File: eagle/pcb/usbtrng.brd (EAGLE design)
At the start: 61 x 30.5 mm, 37 parts, among them IC1 FT232RL, IC2 ATMEGA88, IC3 XC9572XL VQ44, IC4 LT1763CS8-3.3, J1 CON_HEADER_2X03-PTH, J2 CON_HEADER_1X06-PTH, J3 CON_HEADER_1X05-PTH, J5 CON_HEADER_1X01-PTH, J7 CON_HEADER_1X01-PTH, J8 CON_HEADER_1X01-PTH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

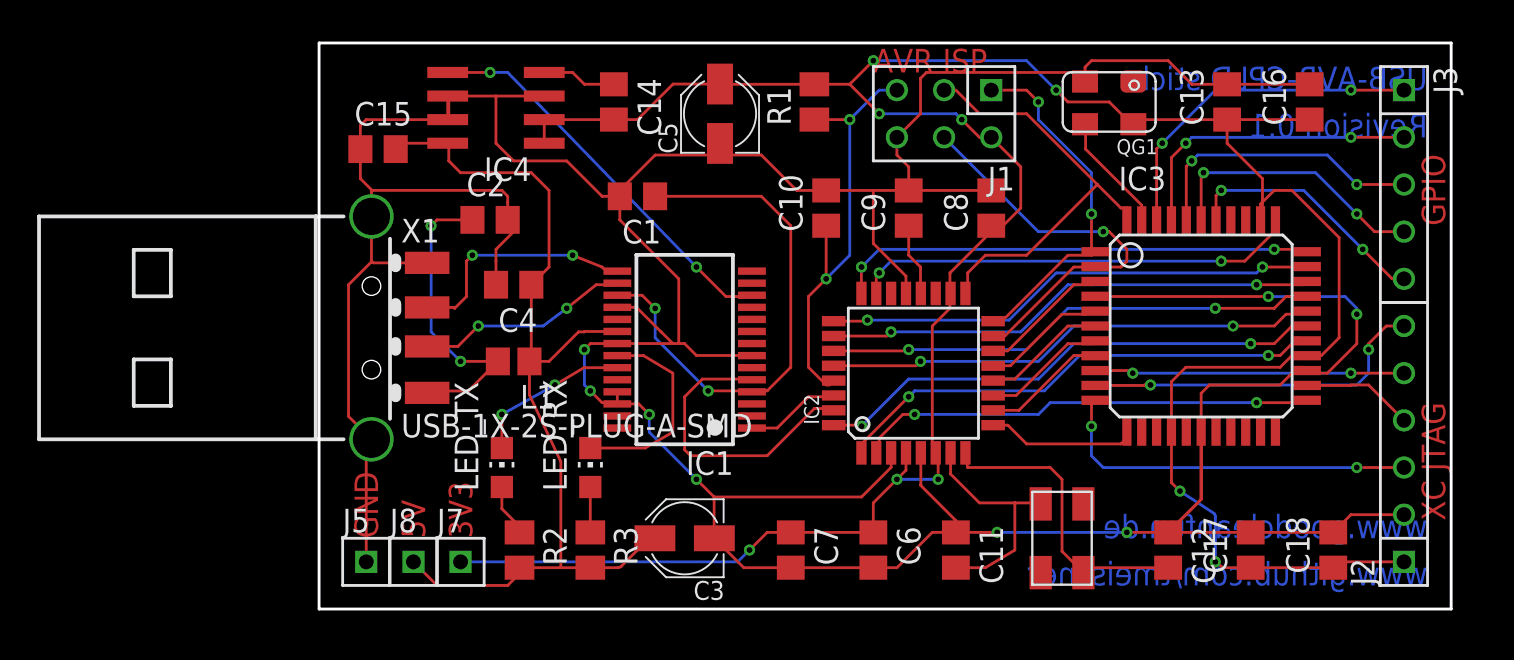
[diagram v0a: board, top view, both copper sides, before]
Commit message: major revision of board layout
* better signal routing around ft232rl
* better placement of blockng capacitors
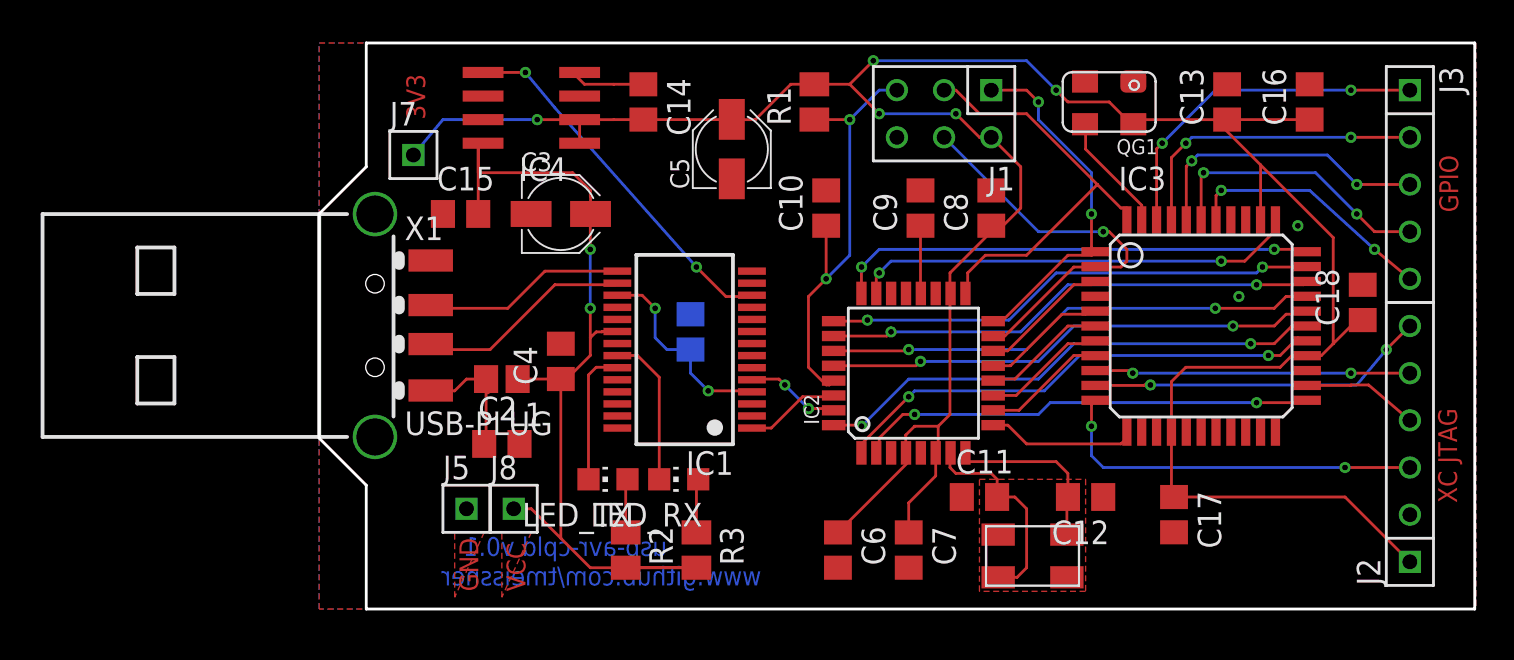
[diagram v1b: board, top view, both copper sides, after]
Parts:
- X1: value USB-1X-2S-PLUG-A-SMD -> USB-PLUG
- moved J7 22.1 mm to (5.08, 24.4)
- moved C3 18.7 mm to (13.0, 21.3), turned to 0 degrees
- moved C18 13.4 mm to (56.2, 16.5)
- moved C2 12.1 mm to (9.84, 8.89)
- moved C1 7.84 mm to (20.0, 14.9), flipped to the bottom, turned to 90 degrees
- moved C7 6.35 mm to (31.8, 3.17)
- moved J5 6.11 mm to (7.94, 5.40)
- moved J8 6.11 mm to (10.5, 5.40)
- moved LED_TX 5.75 mm to (15.6, 6.99), turned to 90 degrees
- moved R2 5.72 mm to (16.5, 3.17)
- moved R3 5.71 mm to (20.3, 3.17)
- moved C15 5.65 mm to (7.62, 21.3)
- moved C12 5.28 mm to (41.3, 6.03), turned to 180 degrees
- moved C4 4.85 mm to (13.0, 13.3), turned to 90 degrees
- moved LED_RX 4.80 mm to (19.4, 6.99), turned to 90 degrees
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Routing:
- net GND: track 257.4 -> 0.00 mm, vias 8 -> 2
- net N$6: track 28.5 -> 11.1 mm
- net FT_RX: track 16.1 -> 5.38 mm, vias 0 -> 2
- net N$4: track 18.0 -> 7.73 mm, vias 2 -> 0
- net +3V3: track 155.5 -> 147.6 mm, vias 9 -> 5
- net N$11: track 16.3 -> 9.50 mm
- net N$9: track 11.1 -> 8.24 mm
- net N$1: track 12.9 -> 11.2 mm, vias 2 -> 0
- net FT_#SLEEP: track 21.5 -> 19.9 mm
- net VCC: track 52.9 -> 51.4 mm, vias 0 -> 2
- net N$8: track 8.69 -> 7.35 mm, vias 2 -> 0
- net N$10: track 12.6 -> 11.6 mm
- net N$5: track 2.45 -> 3.32 mm
- net N$7: track 3.60 -> 2.96 mm
- net XC_TMS: track 18.9 -> 18.4 mm
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- added copper zone on layer 1, net GND
- added copper zone on layer 16, net GND
- added copper zone on layer 1, net N$19
- added copper zone on layer 1, net N$20
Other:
- board size 61 x 30.5 mm -> 62.2 x 30.5 mm
- board text added: "VCC"
- board text added: "usb-avr-cpld v0.1"
- board text removed: "5V"
- board text removed: "AVR ISP"
- board text removed: "Revision 0.1"
- board text removed: "USB-AVR-CPLD stick"
- board text removed: "www.goodcleanfun.de"

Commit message: This is the revision, that is manufactured at q-print, v.0.1
* integrated 32 Mbit SPI-Flash, connected to the CPLD
* The rx/tx leds are now powerd by VCCIO
* further layout optimisations
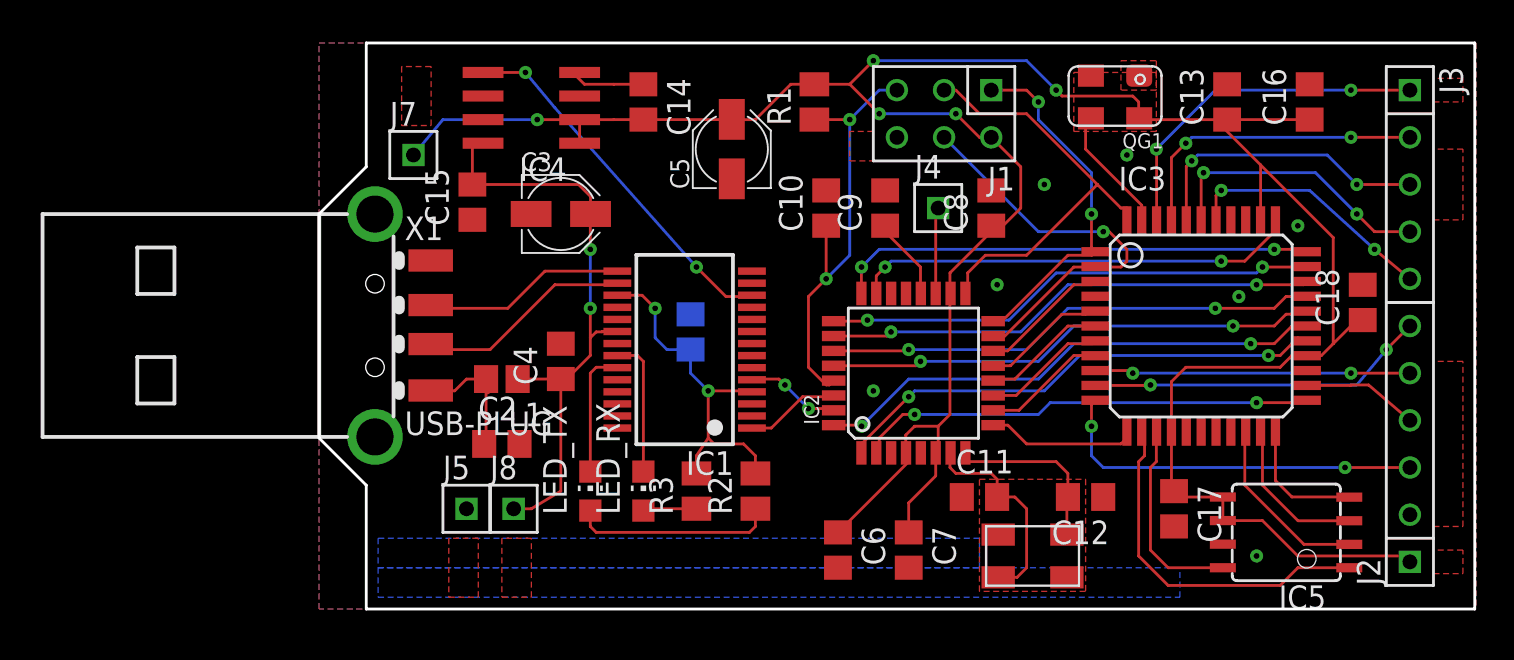
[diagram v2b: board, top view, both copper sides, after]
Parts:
- added IC5: AT45DB161D-SU, atmel:8S2
- added J4: CON_HEADER_1X01-PTH, dp_devices:M1X1
- R2, R3: value 1k -> 68
- moved R2 7.67 mm to (23.5, 6.35), turned to 90 degrees
- moved R3 3.17 mm to (20.3, 6.35), turned to 90 degrees
- moved LED_RX 2.01 mm to (17.5, 6.35), turned to 0 degrees
- moved C9 1.90 mm to (30.5, 21.6)
- moved LED_TX 1.14 mm to (14.6, 6.35), turned to 0 degrees
- moved C15 0.90 mm to (8.26, 21.9), turned to 90 degrees
- moved QG1 0.45 mm to (42.9, 27.6)
- moved C17 0.32 mm to (46.0, 5.40)
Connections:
- new net FLASH_#CS: IC3.22, IC5.4
- new net FLASH_#RST: IC3.21, IC5.3
- new net FLASH_MISO: IC3.14, IC5.8
- new net FLASH_MOSI: IC3.13, IC5.1
- new net FLASH_SCK: IC3.20, IC5.2
- new net N$18: IC2.19, J4.1
- net +3V3: now also IC5.5, IC5.6
- net GND: now also IC5.7
- net N$6: now also R2.2, R3.2
- net VCC: no longer R2.2, R3.2
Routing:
- net FLASH_MOSI: track 0.00 -> 19.3 mm
- net VCC: track 51.4 -> 33.8 mm
- net FLASH_MISO: track 0.00 -> 10.8 mm
- net FLASH_SCK: track 0.00 -> 9.86 mm
- net N$6: track 11.1 -> 19.6 mm
- net FLASH_#RST: track 0.00 -> 8.35 mm
- net N$7: track 2.96 -> 11.0 mm
- net FLASH_#CS: track 0.00 -> 7.07 mm
- net N$18: track 0.00 -> 4.65 mm
- net +3V3: track 147.6 -> 149.1 mm
- net N$3: track 3.66 -> 4.44 mm
- net N$9: track 8.24 -> 7.47 mm
- added copper zone on layer 1, net N$21
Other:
- board text added: "(c) 2012 by T. Meissner - www.github.com/tmeissner"
- board text added: "1"
- board text added: "6"
- board text added: "CPLD JTAG"
- board text added: "USB-AVR-CPLD experimental board v0.1"
- board text removed: "XC JTAG"
- board text removed: "usb-avr-cpld v0.1"
- board text removed: "www.github.com/tmeissner"
